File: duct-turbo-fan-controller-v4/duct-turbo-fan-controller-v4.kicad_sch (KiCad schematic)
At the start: 38 parts, among them J1 Screw_Terminal_01x04, J2 Conn_01x04, J3 USB_OTG, J4 AudioJack4, J7 Conn_01x04, Q1 MMBT3904, Q2 BSS84, SW1 SW_Push, SW2 SW_Push, U2 BME680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

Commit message: Move to smaller inductor as buck switch is 1MHz
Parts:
- L1: footprint Inductor_SMD:L_6.3x6.3_H3 -> Inductor_SMD:L_Bourns-SRN4018
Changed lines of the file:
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@@
 			)
 		)
-		(property "Footprint" "Inductor_SMD:L_6.3x6.3_H3"
+		(property "Footprint" "Inductor_SMD:L_Bourns-SRN4018"
 			(at 140.97 173.99 0)
 			(effects

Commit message: Add label for pull up. Add tag.
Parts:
- R14: value R_Small -> 10K
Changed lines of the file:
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@@
 			)
 		)
-		(property "Value" "R_Small"
+		(property "Value" "10K"
 			(at 101.6 175.2599 0)
 			(effects

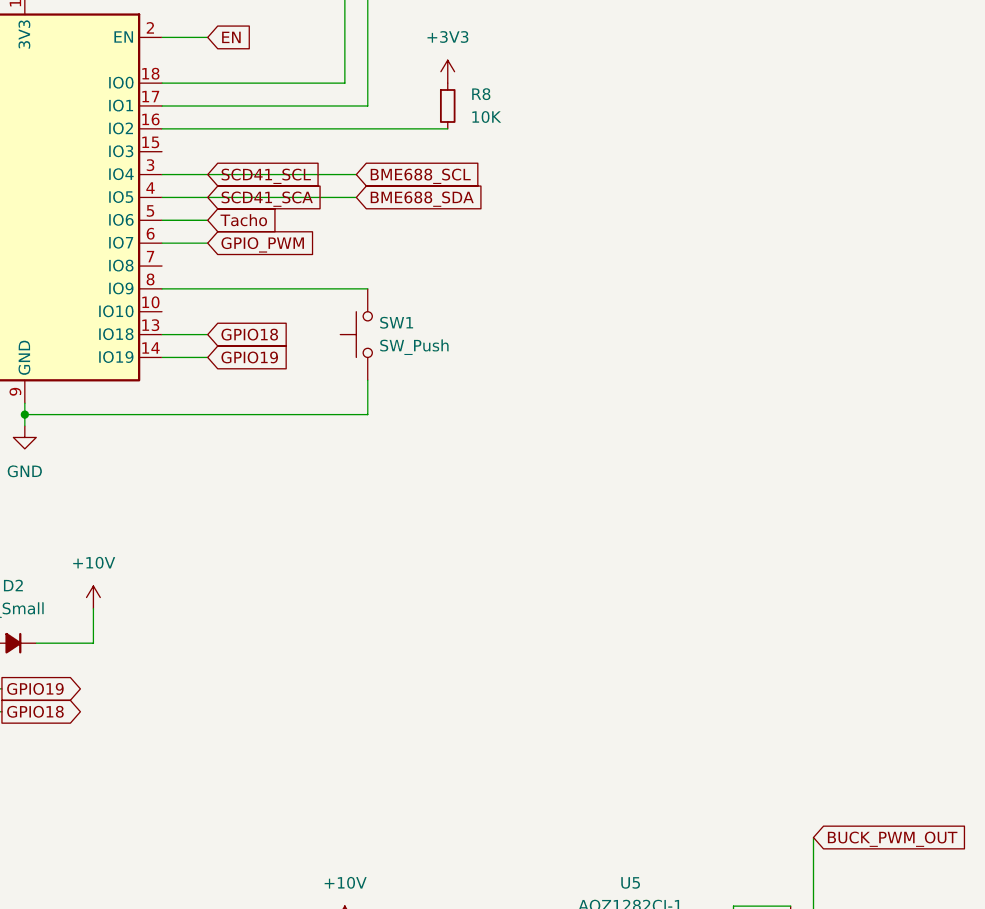
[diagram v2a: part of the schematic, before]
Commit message: Add scd41 to the board.
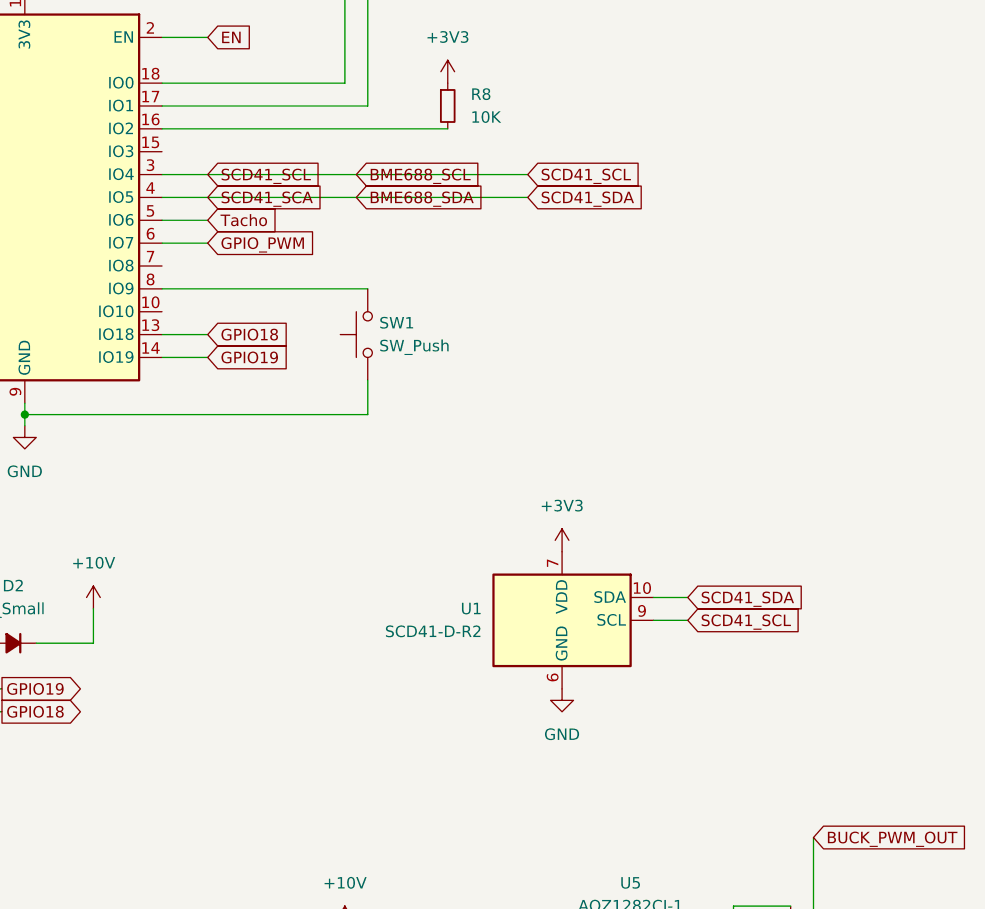
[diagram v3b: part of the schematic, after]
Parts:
- added U1: SCD41-D-R2, Sensor:Sensirion_SCD4x-1EP_10.1x10.1mm_P1.25mm_EP4.8x4.8mm, symbol Sensor_Gas:SCD41-D-R2
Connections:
- net +3V3: now also U1.19 (VDD), U1.7 (VDD)
- net BME688_SCL: now also U1.9 (SCL)
- net BME688_SDA: now also U1.10 (SDA)
- net GND: now also U1.20 (GND), U1.21 (GND), U1.6 (GND)

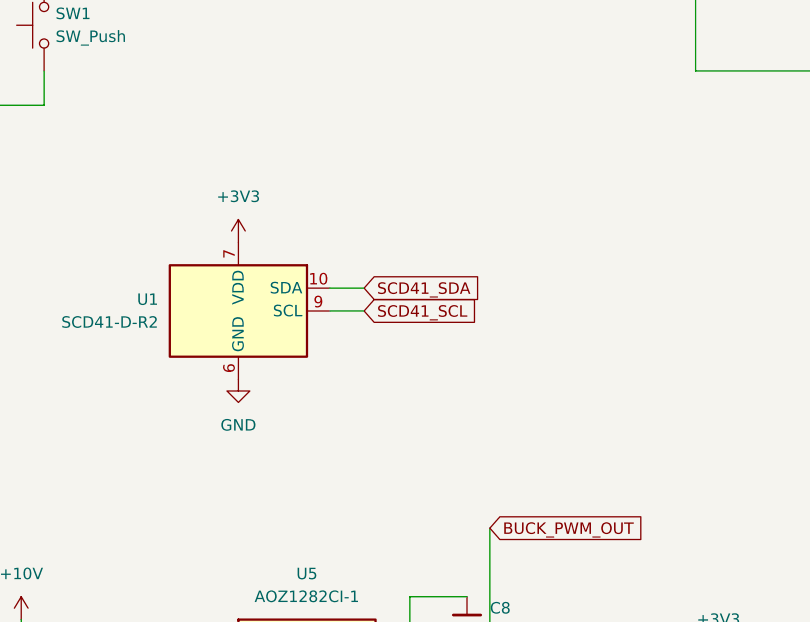
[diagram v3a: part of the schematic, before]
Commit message: Add capacitance close to sc41 for ripple reduction.
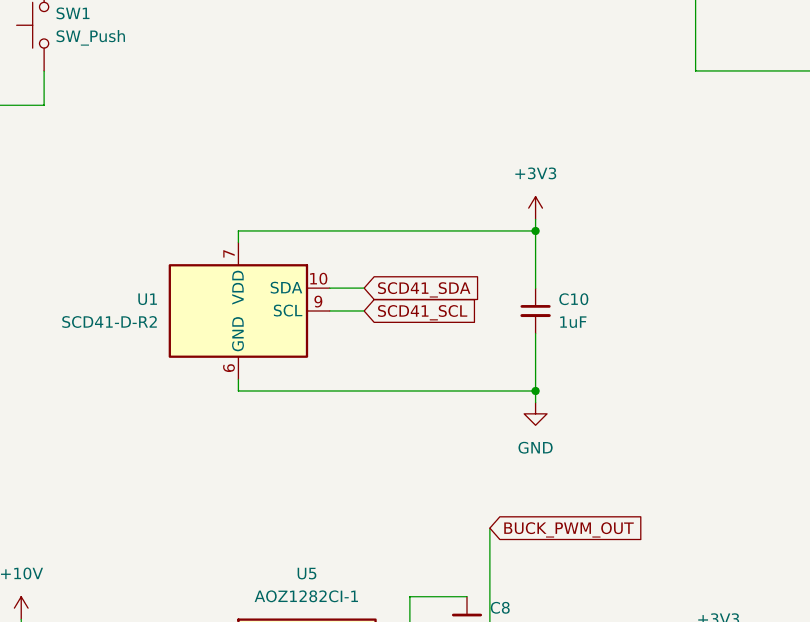
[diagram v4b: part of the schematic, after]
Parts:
- added C10: 1uF, Capacitor_SMD:C_1206_3216Metric_Pad1.33x1.80mm_HandSolder, symbol Device:C_Small
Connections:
- net +3V3: now also C10.1
- net GND: now also C10.2
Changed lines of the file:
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@@
 	)
 	(junction
+		(at 142.24 125.73)
+		(diameter 0)
+		(color 0 0 0 0)
+	)
+	(junction
 		(at 64.77 26.67)
 		(diameter 0)
@@
 	)
 	(junction
+		(at 142.24 143.51)
+		(diameter 0)
+		(color 0 0 0 0)
+	)
+	(junction
 		(at 224.79 161.29)
 		(diameter 0)
@@
 	(wire
 		(pts
+			(xy 142.24 125.73) (xy 109.22 125.73)
+		)
+		(stroke
+			(width 0)
+			(type default)
+		)
+	)
+	(wire
+		(pts
 			(xy 87.63 111.76) (xy 49.53 111.76)
 		)
@@
 	(wire
 		(pts
+			(xy 109.22 125.73) (xy 109.22 127)
+		)
+		(stroke
+			(width 0)
+			(type default)
+		)
+	)
+	(wire
+		(pts
 			(xy 31.75 152.4) (xy 31.75 156.21)
 		)
@@
 	(wire
 		(pts
+			(xy 109.22 143.51) (xy 109.22 142.24)
+		)
+		(stroke
+			(width 0)
+			(type default)
+		)
+	)
+	(wire
+		(pts
 			(xy 53.34 36.83) (xy 64.77 36.83)
 		)
@@
 	(wire
 		(pts
+			(xy 142.24 144.78) (xy 142.24 143.51)
+		)
+		(stroke
+			(width 0)
+			(type default)
+		)
+	)
+	(wire
+		(pts
 			(xy 163.83 31.75) (xy 163.83 30.48)
 		)
@@
 	(wire
 		(pts
+			(xy 142.24 124.46) (xy 142.24 125.73)
+		)
+		(stroke
+			(width 0)
+			(type default)
+		)
+	)
+	(wire
+		(pts
 			(xy 215.9 88.9) (xy 223.52 88.9)
 		)
@@
 	(wire
 		(pts
+			(xy 142.24 125.73) (xy 142.24 132.08)
+		)
+		(stroke
+			(width 0)
+			(type default)
+		)
+	)
+	(wire
+		(pts
 			(xy 196.85 154.94) (xy 196.85 161.29)
 		)
@@
 	(wire
 		(pts
+			(xy 142.24 137.16) (xy 142.24 143.51)
+		)
+		(stroke
+			(width 0)
+			(type default)
+		)
+	)
+	(wire
+		(pts
 			(xy 119.38 134.62) (xy 123.19 134.62)
 		)
@@
 	(wire
 		(pts
+			(xy 142.24 143.51) (xy 109.22 143.51)
+		)
+		(stroke
+			(width 0)
+			(type default)
+		)
+	)
+	(wire
+		(pts
 			(xy 128.27 166.37) (xy 134.62 166.37)
 		)
@@
 	)
 	(symbol
+		(lib_id "Device:C_Small")
+		(at 142.24 134.62 0)
+		(unit 1)
+		(exclude_from_sim no)
+		(in_bom yes)
+		(on_board yes)
+		(dnp no)
+		(property "Reference" "C10"
+			(at 144.78 133.3562 0)
+			(effects
+				(font
+					(size 1.27 1.27)
+				)
+				(justify left)
+			)
+		)
+		(property "Value" "1uF"
+			(at 144.78 135.8962 0)
+			(effects
+				(font
+					(size 1.27 1.27)
+				)
+				(justify left)
+			)
+		)
+		(property "Footprint" "Capacitor_SMD:C_1206_3216Metric_Pad1.33x1.80mm_HandSolder"
+			(at 142.24 134.62 0)
+			(effects
+				(font
+					(size 1.27 1.27)
+				)
+				(hide yes)
+			)
+		)
+		(property "Datasheet" "~"
+			(at 142.24 134.62 0)
+			(effects
+				(font
+					(size 1.27 1.27)
+				)
+				(hide yes)
+			)
+		)
+		(property "Description" "Unpolarized capacitor, small symbol"
+			(at 142.24 134.62 0)
+			(effects
+				(font
+					(size 1.27 1.27)
+				)
+				(hide yes)
+			)
+		)
+		(pin "1"
+		)
+		(pin "2"
+		)
+		(instances
+			(project ""
+				(path "/f7200693-aa8c-4dc9-bbe2-9e962fa196ea"
+					(reference "C10")
+					(unit 1)
+				)
+			)
+		)
+	)
+	(symbol
 		(lib_id "power:+3.3V")
 		(at 83.82 24.13 0)
@@
 	(symbol
 		(lib_id "power:GND")
-		(at 109.22 142.24 0)
+		(at 142.24 144.78 0)
 		(unit 1)
 		(exclude_from_sim no)
@@
 		(fields_autoplaced yes)
 		(property "Reference" "#PWR015"
-			(at 109.22 148.59 0)
+			(at 142.24 151.13 0)
 			(effects
 				(font
@@
 		)
 		(property "Value" "GND"
-			(at 109.22 147.32 0)
+			(at 142.24 149.86 0)
 			(effects
 				(font
@@
 		)
 		(property "Footprint" ""
-			(at 109.22 142.24 0)
+			(at 142.24 144.78 0)
 			(effects
 				(font
@@
 		)
 		(property "Datasheet" ""
-			(at 109.22 142.24 0)
+			(at 142.24 144.78 0)
 			(effects
 				(font
@@
 		)
 		(property "Description" ""
-			(at 109.22 142.24 0)
+			(at 142.24 144.78 0)
 			(effects
 				(font
@@
 	(symbol
 		(lib_id "power:+3.3V")
-		(at 109.22 127 0)
+		(at 142.24 124.46 0)
 		(unit 1)
 		(exclude_from_sim no)
@@
 		(fields_autoplaced yes)
 		(property "Reference" "#PWR016"
-			(at 109.22 130.81 0)
+			(at 142.24 128.27 0)
 			(effects
 				(font
@@
 		)
 		(property "Value" "+3V3"
-			(at 109.22 121.92 0)
+			(at 142.24 119.38 0)
 			(effects
 				(font
@@
 		)
 		(property "Footprint" ""
-			(at 109.22 127 0)
+			(at 142.24 124.46 0)
 			(effects
 				(font
@@
 		)
 		(property "Datasheet" ""
-			(at 109.22 127 0)
+			(at 142.24 124.46 0)
 			(effects
 				(font
@@
 		)
 		(property "Description" ""
-			(at 109.22 127 0)
+			(at 142.24 124.46 0)
 			(effects
 				(font

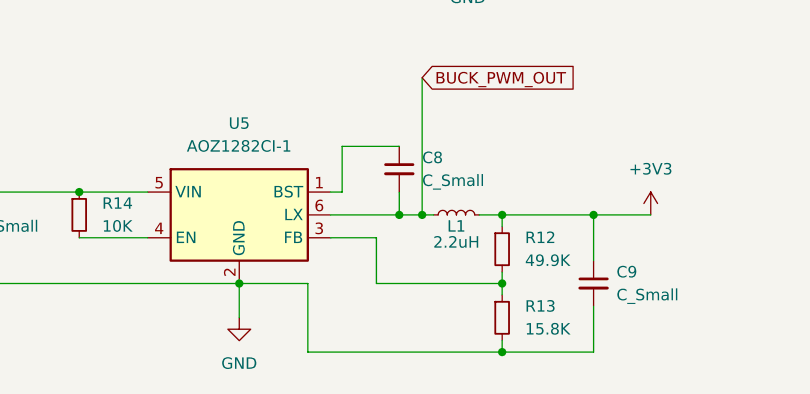
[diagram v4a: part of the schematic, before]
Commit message: Add missing schottky diode on the pwm output
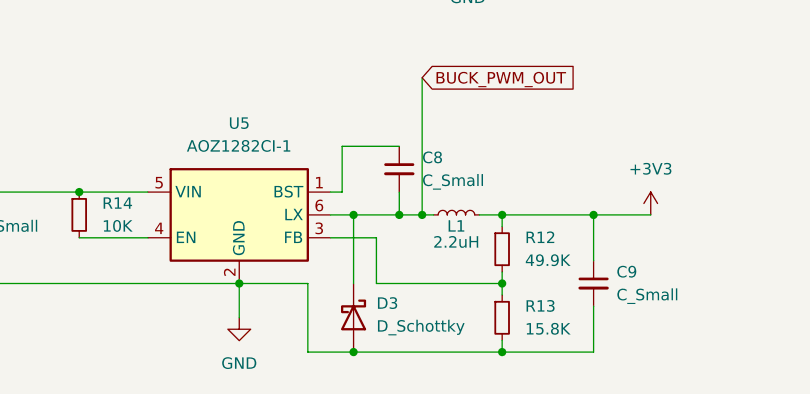
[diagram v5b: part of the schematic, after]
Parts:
- added D3: D_Schottky, Diode_SMD:D_SOD-323_HandSoldering, symbol Device:D_Schottky
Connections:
- net BUCK_PWM_OUT: now also D3.1 (K)
- net GND: now also D3.2 (A)
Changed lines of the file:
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@@
+	)
+	(junction
+		(at 129.54 189.23)
+		(diameter 0)
+		(color 0 0 0 0)
 	)
 	(junction
@@
 	)
 	(junction
+		(at 129.54 173.99)
+		(diameter 0)
+		(color 0 0 0 0)
+	)
+	(junction
 		(at 224.79 120.65)
 		(diameter 0)
@@
 	(wire
 		(pts
+			(xy 129.54 189.23) (xy 124.46 189.23)
+		)
+		(stroke
+			(width 0)
+			(type default)
+		)
+	)
+	(wire
+		(pts
 			(xy 215.9 120.65) (xy 224.79 120.65)
 		)
@@
 	(wire
 		(pts
-			(xy 146.05 189.23) (xy 124.46 189.23)
+			(xy 146.05 189.23) (xy 129.54 189.23)
 		)
 		(stroke
@@
 	(wire
 		(pts
+			(xy 129.54 173.99) (xy 134.62 173.99)
+		)
+		(stroke
+			(width 0)
+			(type default)
+		)
+	)
+	(wire
+		(pts
 			(xy 156.21 189.23) (xy 146.05 189.23)
 		)
@@
 	(wire
 		(pts
+			(xy 129.54 173.99) (xy 129.54 181.61)
+		)
+		(stroke
+			(width 0)
+			(type default)
+		)
+	)
+	(wire
+		(pts
 			(xy 199.39 83.82) (xy 200.66 83.82)
 		)
@@
 	(wire
 		(pts
-			(xy 127 173.99) (xy 134.62 173.99)
+			(xy 127 173.99) (xy 129.54 173.99)
 		)
 		(stroke
@@
 					(unit 1)
 				)
+			)
+		)
+	)
+	(symbol
+		(lib_id "Device:D_Schottky")
+		(at 129.54 185.42 270)
+		(unit 1)
+		(exclude_from_sim no)
+		(in_bom yes)
+		(on_board yes)
+		(dnp no)
+		(fields_autoplaced yes)
+		(property "Reference" "D3"
+			(at 132.08 183.8324 90)
+			(effects
+				(font
+					(size 1.27 1.27)
+				)
+				(justify left)
+			)
+		)
+		(property "Value" "D_Schottky"
+			(at 132.08 186.3724 90)
+			(effects
+				(font
+					(size 1.27 1.27)
+				)
+				(justify left)
+			)
+		)
+		(property "Footprint" "Diode_SMD:D_SOD-323_HandSoldering"
+			(at 129.54 185.42 0)
+			(effects
+				(font
+					(size 1.27 1.27)
+				)
+				(hide yes)
+			)
+		)
+		(property "Datasheet" "~"
+			(at 129.54 185.42 0)
+			(effects
+				(font
+					(size 1.27 1.27)
+				)
+				(hide yes)
+			)
+		)
+		(property "Description" "Schottky diode"
+			(at 129.54 185.42 0)
+			(effects
+				(font
+					(size 1.27 1.27)
+				)
+				(hide yes)
+			)
+		)
+		(pin "2"
+		)
+		(pin "1"
+		)
+		(instances
+			(project ""
+				(path "/f7200693-aa8c-4dc9-bbe2-9e962fa196ea"
+					(reference "D3")
+					(unit 1)
+				)

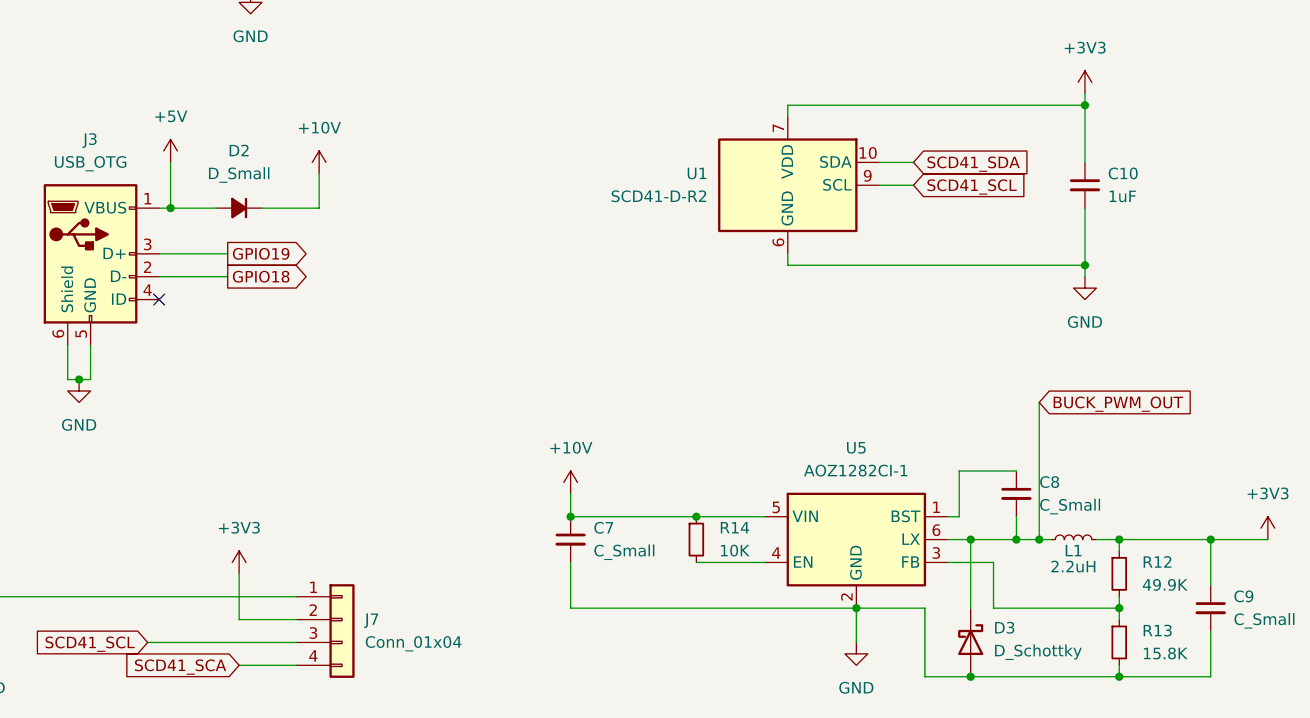
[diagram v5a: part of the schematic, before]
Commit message: Updates to the labels on diodes and inductors
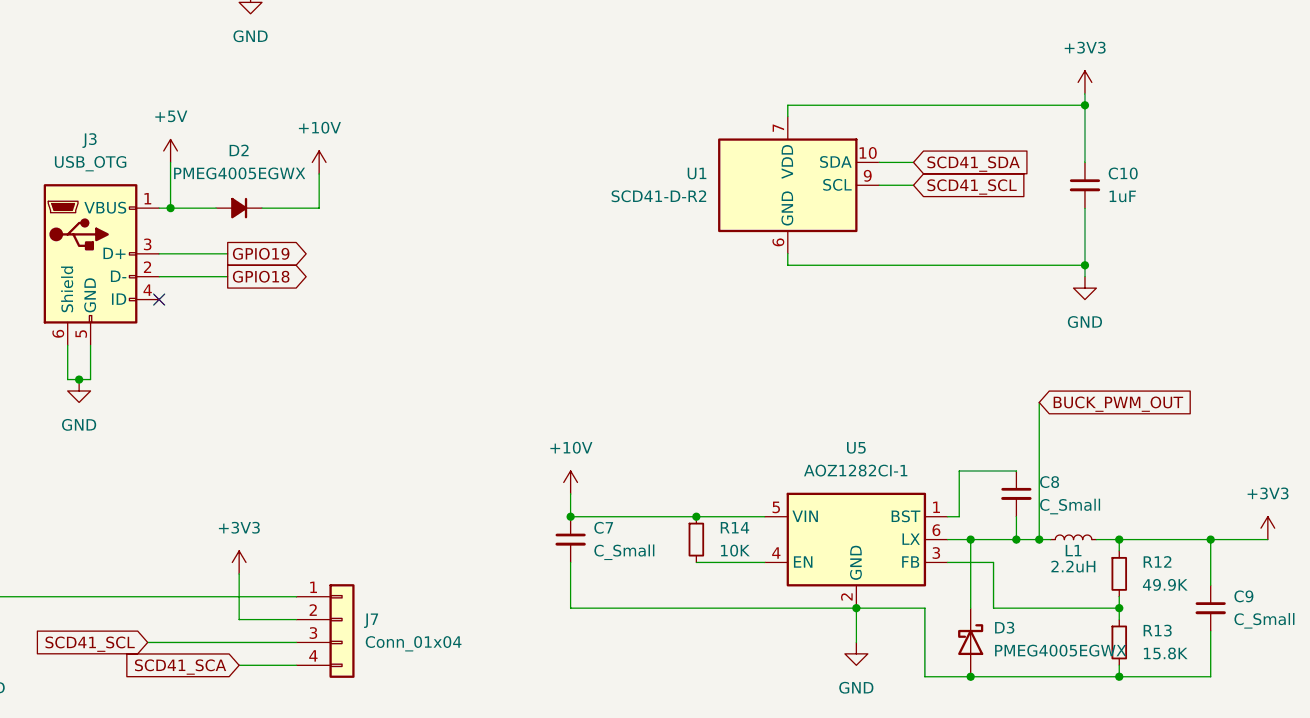
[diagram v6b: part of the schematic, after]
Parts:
- D2: value D_Small -> PMEG4005EGWX
- D3: value D_Schottky -> PMEG4005EGWX
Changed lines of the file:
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@@
 			)
 		)
-		(property "Value" "D_Schottky"
+		(property "Value" "PMEG4005EGWX"
 			(at 132.08 186.3724 90)
 			(effects
@@
 			)
 		)
-		(property "Datasheet" "~"
+		(property "Datasheet" "https://www.bourns.com/docs/Product-Datasheets/SRN4018.pdf"
 			(at 140.97 173.99 0)
 			(effects
@@
 			)
 		)
-		(property "Value" "D_Small"
+		(property "Value" "PMEG4005EGWX"
 			(at 48.26 133.35 0)
 			(effects
